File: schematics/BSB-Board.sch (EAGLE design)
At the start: 23 parts, among them Q1 BC 547A, Q11 BC 557A, Q12 BC 547A, U1 4N25, U2 4N25

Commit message: Bugfixes
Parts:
- removed SJ4_RPI: Close for RPi, jumper:SJ
- added SJ2_RPI: Close for RPi, jumper:SJ
- renumbered ARD_SUP to ARD_5V
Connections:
- net N$11 renamed ARD_PI_TXD
- net A14-RXD-ARD: now also ARD_8-15.7; no longer ARD_8-15.2
- net A15-TXD-ARD: now also ARD_8-15.8; no longer ARD_8-15.1
- net GND-ARD: now also SJ2_RPI.2; no longer SJ3_RPI.2
- net GPIO18-3V3-PI: now also SJ3_RPI.1; no longer SJ4_RPI.1
- net PIN6-GND-PI: now also SJ2_RPI.1; no longer SJ3_RPI.1
- net VCC: now also SJ3_RPI.2; no longer SJ4_RPI.2
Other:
- note added: "06-GND"
- note added: "08-TXD"
- note added: "10-RXD"
- note added: "12-3V3"
- note added: "A14-RXD"
- note added: "A15-TXD"
- note added: "CL+/DB"
- note added: "CL-/MB"
- note added: "R11-13 and Q11-12 only required for Raspberry Pi board"
- moved on the sheet: ARD_23-53, ARD_8-15, ARD_GND, D1, D2, Q1, Q12, R1, R12, R2, R3, SJ3_RPI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

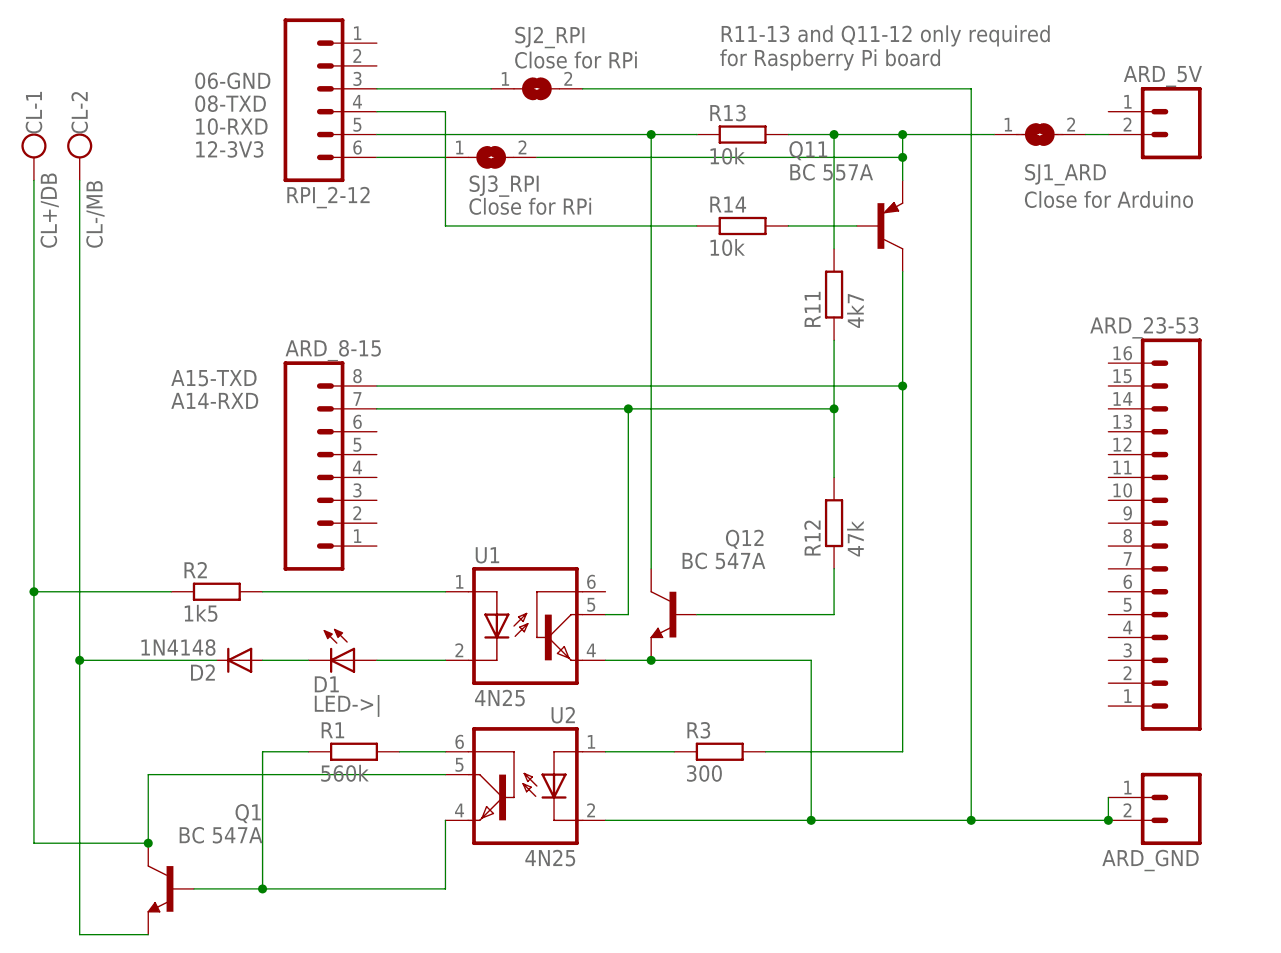
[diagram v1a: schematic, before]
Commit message: Clarified layout
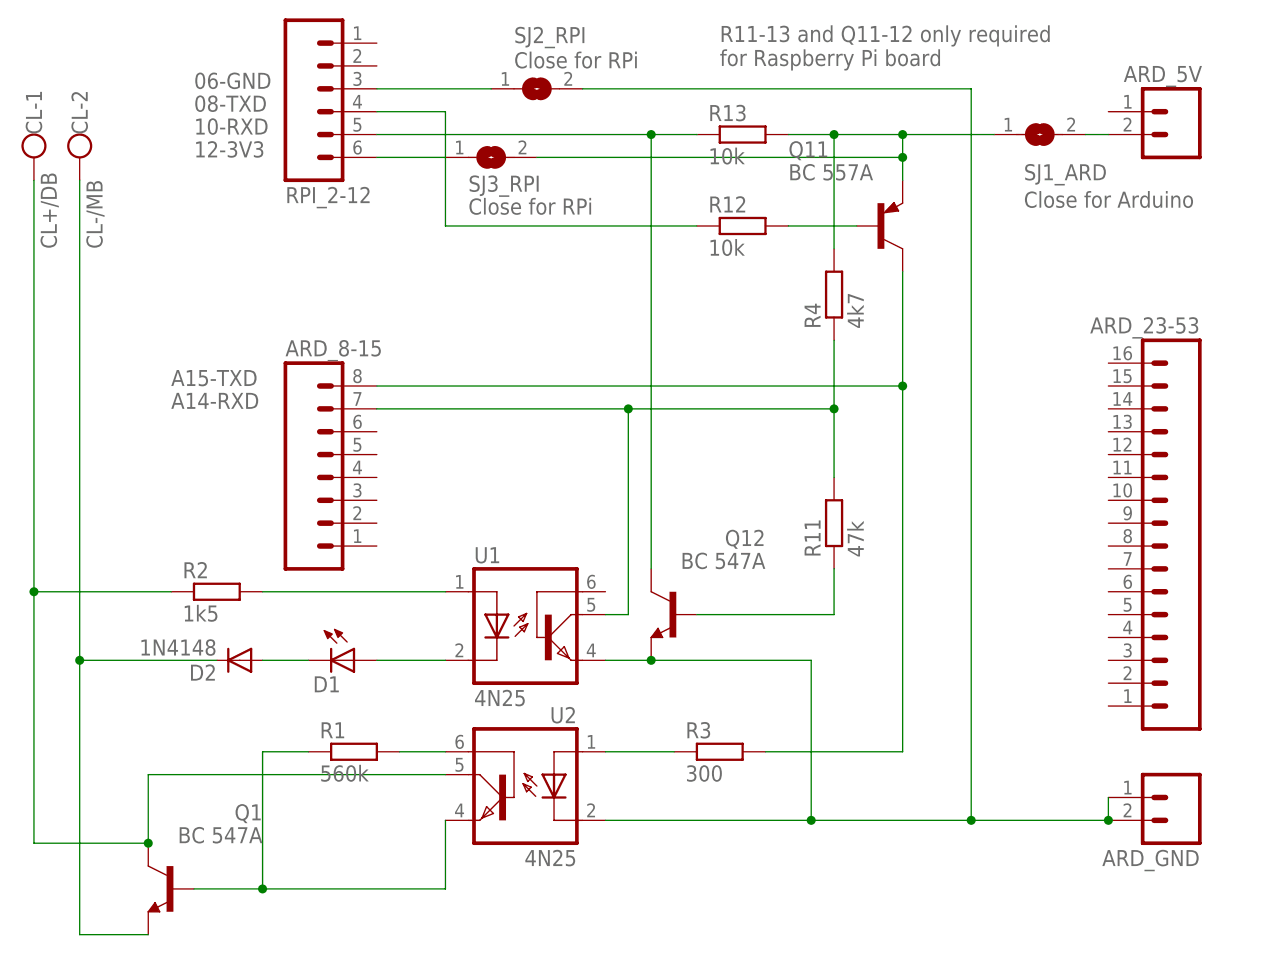
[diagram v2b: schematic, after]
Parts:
- removed R14: 10k, resistor:R-EU_0204_7
- added R4: 4k7, resistor:R-EU_0204_7
- D1: value LED->| -> (none)
- R11: value 4k7 -> 47k
- R12: value 47k -> 10k
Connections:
- net A14-RXD-ARD: now also R11.2, R4.1; no longer R11.1, R12.2
- net GPIO14-TXD-PI: now also R12.1; no longer R14.1
- net N$6: now also R11.1; no longer R12.1
- net N$9: now also R12.2; no longer R14.2
- net VCC: now also R4.2; no longer R11.2
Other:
- moved on the sheet: R11, R12
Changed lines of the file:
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@@
 <part name="R1" library="resistor" deviceset="R-EU_" device="0204_7" value="560k"/>
 <part name="R3" library="resistor" deviceset="R-EU_" device="0204_7" value="300"/>
-<part name="D1" library="led" deviceset="LED" device="SQR2X5" value="LED-&gt;|"/>
+<part name="D1" library="led" deviceset="LED" device="SQR2X5"/>
 <part name="CL" library="con-wago-500" deviceset="W237-102" device=""/>
 <part name="Q12" library="transistor" deviceset="*-NPN-" device="TO92-CBE" technology="BC547" value="BC 547A"/>
-<part name="R12" library="resistor" deviceset="R-EU_" device="0204_7" value="47k"/>
-<part name="R11" library="resistor" deviceset="R-EU_" device="0204_7" value="4k7"/>
-<part name="R14" library="resistor" deviceset="R-EU_" device="0204_7" value="10k"/>
+<part name="R11" library="resistor" deviceset="R-EU_" device="0204_7" value="47k"/>
+<part name="R4" library="resistor" deviceset="R-EU_" device="0204_7" value="4k7"/>
+<part name="R12" library="resistor" deviceset="R-EU_" device="0204_7" value="10k"/>
 <part name="R13" library="resistor" deviceset="R-EU_" device="0204_7" value="10k"/>
 <part name="Q11" library="transistor-neu-to92" deviceset="*-PNP-" device="TO92-CBE" value="BC 557A"/>
@@
 <instance part="CL" gate="-2" x="109.22" y="154.94" rot="R270"/>
 <instance part="Q12" gate="G$1" x="175.26" y="101.6" rot="MR0"/>
-<instance part="R12" gate="G$1" x="193.04" y="111.76" rot="R90"/>
-<instance part="R11" gate="G$1" x="193.04" y="137.16" rot="R90"/>
-<instance part="R14" gate="G$1" x="182.88" y="144.78"/>
+<instance part="R11" gate="G$1" x="193.04" y="111.76" rot="R90"/>
+<instance part="R4" gate="G$1" x="193.04" y="137.16" rot="R90"/>
+<instance part="R12" gate="G$1" x="182.88" y="144.78"/>
 <instance part="R13" gate="G$1" x="182.88" y="154.94"/>
 <instance part="Q11" gate="G$1" x="198.12" y="144.78"/>
@@
 <pinref part="U1" gate="G$1" pin="COL"/>
 <wire x1="167.64" y1="101.6" x2="170.18" y2="101.6" width="0.1524" layer="91"/>
-<pinref part="R11" gate="G$1" pin="1"/>
-<pinref part="R12" gate="G$1" pin="2"/>
+<pinref part="R4" gate="G$1" pin="1"/>
+<pinref part="R11" gate="G$1" pin="2"/>
 <wire x1="193.04" y1="116.84" x2="193.04" y2="124.46" width="0.1524" layer="91"/>
 <pinref part="ARD_8-15" gate="G$1" pin="7"/>
@@
 <pinref part="Q11" gate="G$1" pin="E"/>
 <wire x1="193.04" y1="154.94" x2="200.66" y2="154.94" width="0.1524" layer="91"/>
-<pinref part="R11" gate="G$1" pin="2"/>
+<pinref part="R4" gate="G$1" pin="2"/>
 <wire x1="193.04" y1="142.24" x2="193.04" y2="154.94" width="0.1524" layer="91"/>
 <wire x1="200.66" y1="149.86" x2="200.66" y2="152.4" width="0.1524" layer="91"/>
@@
 <segment>
 <pinref part="Q11" gate="G$1" pin="B"/>
-<pinref part="R14" gate="G$1" pin="2"/>
+<pinref part="R12" gate="G$1" pin="2"/>
 <wire x1="195.58" y1="144.78" x2="187.96" y2="144.78" width="0.1524" layer="91"/>
 </segment>
@@
 <segment>
 <wire x1="149.86" y1="144.78" x2="149.86" y2="157.48" width="0.1524" layer="91"/>
-<pinref part="R14" gate="G$1" pin="1"/>
+<pinref part="R12" gate="G$1" pin="1"/>
 <wire x1="177.8" y1="144.78" x2="149.86" y2="144.78" width="0.1524" layer="91"/>
 <wire x1="149.86" y1="157.48" x2="142.24" y2="157.48" width="0.1524" layer="91"/>
@@
 <segment>
 <pinref part="Q12" gate="G$1" pin="B"/>
-<pinref part="R12" gate="G$1" pin="1"/>
+<pinref part="R11" gate="G$1" pin="1"/>
 <wire x1="177.8" y1="101.6" x2="193.04" y2="101.6" width="0.1524" layer="91"/>
 <wire x1="193.04" y1="101.6" x2="193.04" y2="106.68" width="0.1524" layer="91"/>
